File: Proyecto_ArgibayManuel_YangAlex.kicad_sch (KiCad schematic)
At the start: 45 parts, among them IC1 LM1117, J1 Conn_01x09, J2 Conn_01x08, K1 RT314012, K2 RT314012, Q1 2N2222, Q2 2N2222, SW1 SW_Push, SW2 SW_Push, SW3 SW_Push, SW4 SW_Push, SW5 SW_Push, SW6 SW_Push, U1 PIC18F258-I_SO, U10 LT1716IS5TRMPBF, U2 DRV8871DDA, U3 DRV8871DDA, U6 MCP2551-I-P, U9 LT1716IS5TRMPBF, X1 DB9, Y1 Crystal

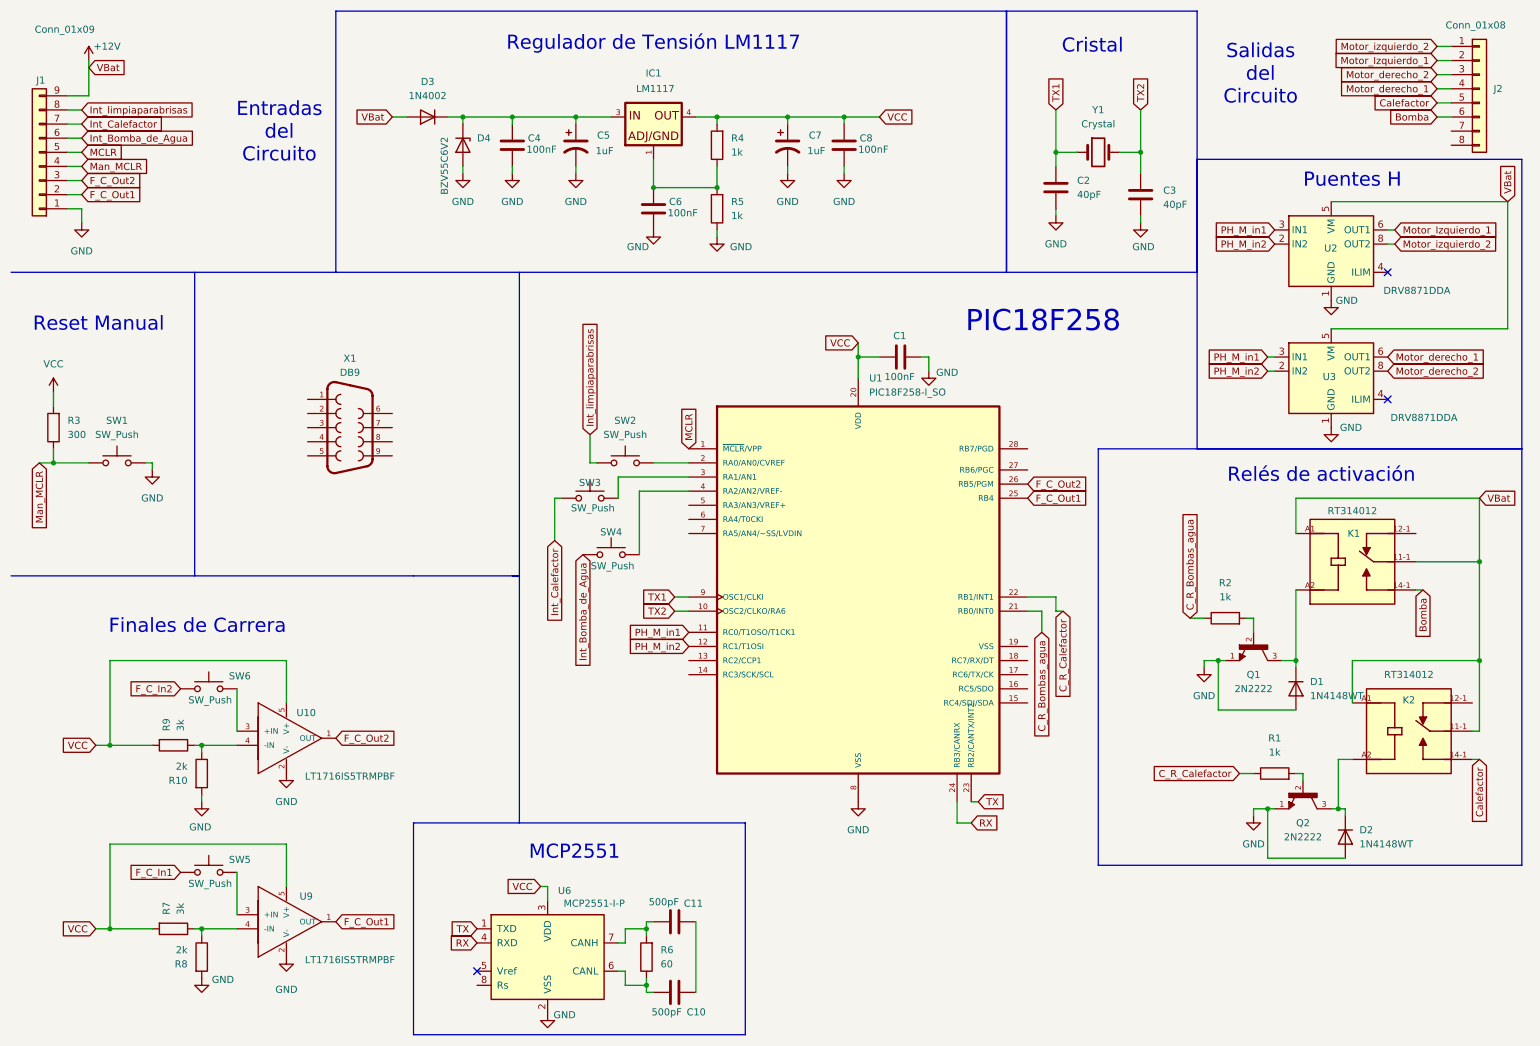
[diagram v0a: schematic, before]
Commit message: Modificación de esquemático y presentación de pptx
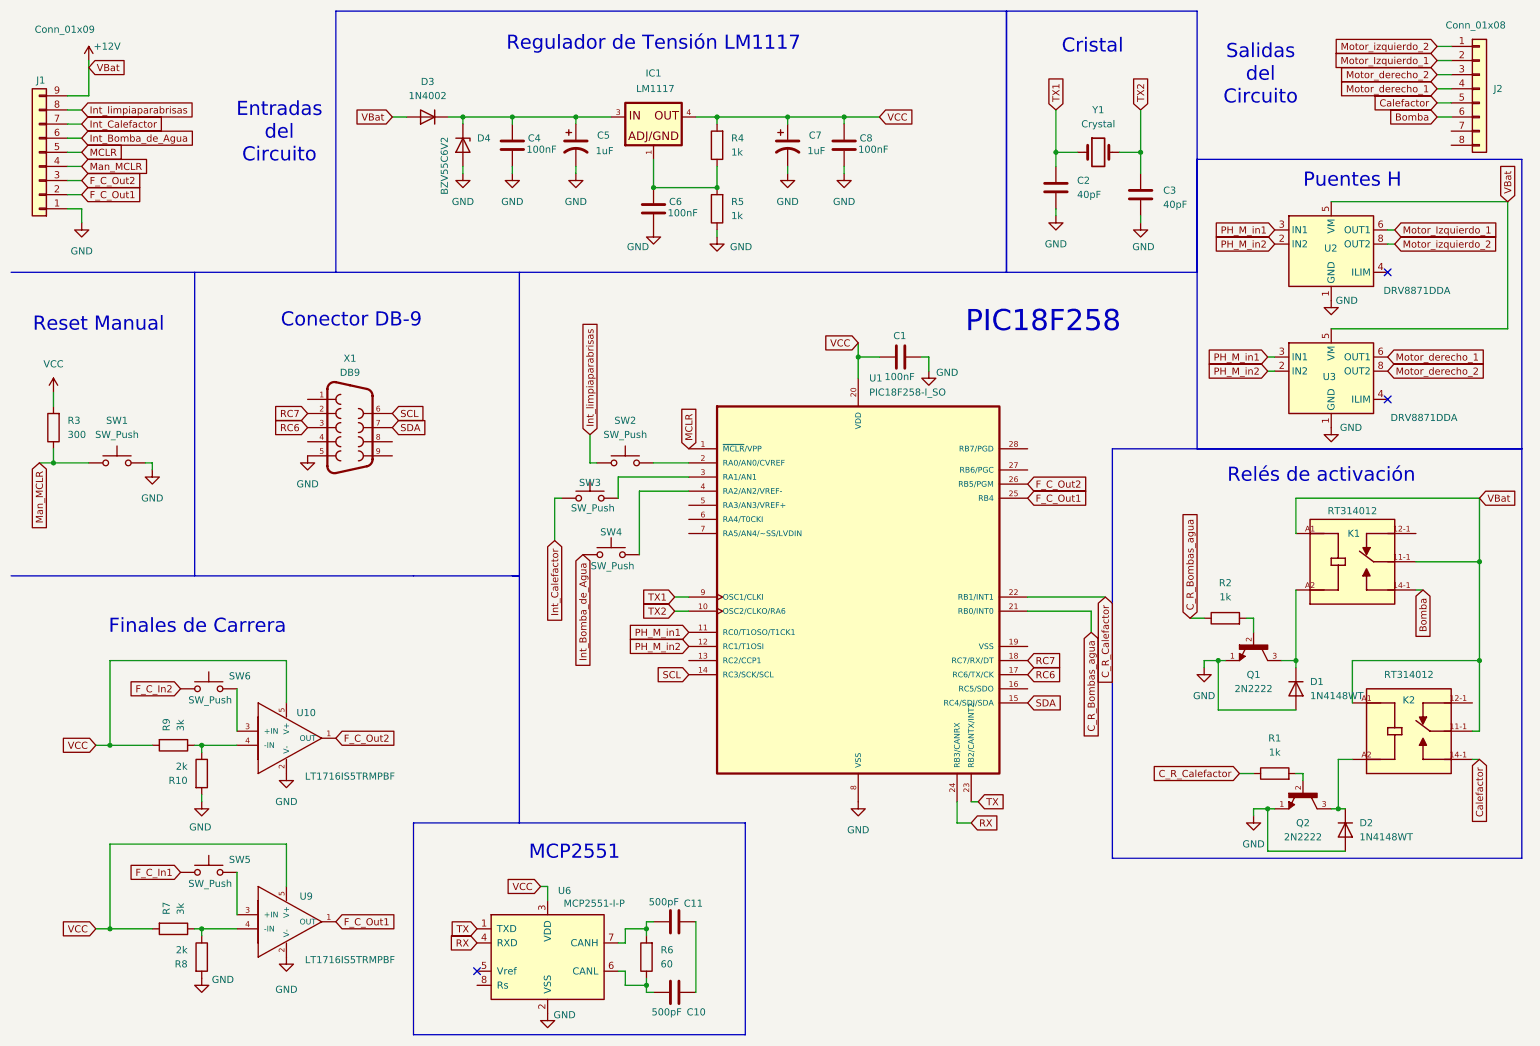
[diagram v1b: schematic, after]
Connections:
- net GND: now also X1.5
- net RC7: now reaches X1.2
- net RC7: now also U1.18 (RC7/RX/DT)
- net RC6: now reaches X1.3
- net RC6: now also U1.17 (RC6/TX/CK)
- net SCL: now reaches X1.6
- net SCL: now also U1.14 (RC3/SCK/SCL)
- net SDA: now reaches X1.7
- net SDA: now also U1.15 (RC4/SDI/SDA)
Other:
- note added: "Conector DB-9"
- company: (none) -> Universidad de Barcelona
- title: (none) -> Proyecto - Limpia Parabrisas
- moved on the sheet: D2
